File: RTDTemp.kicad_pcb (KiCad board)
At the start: 2 copper layers, 114.5 x 60 mm, 102 parts, among them J1 Conn_01x02, J10 Conn_01x02, J11 Conn_01x02, J2 Conn_01x02, J3 Conn_01x02, J4 CAN_In, J5 CAN_Out, J6 Conn_01x02, J7 Conn_01x02, J8 Conn_01x02, J9 Conn_01x02, U1 INA21x, U10 INA21x, U11 INA21x, U12 INA21x, U2 Nucleo_L432KC, U3 PDS1-Sx-Sx, U4 INA21x, U5 ADM3055E, U6 INA21x, U7 CDSOT23-T24CAN, U8 INA21x, U9 INA21x

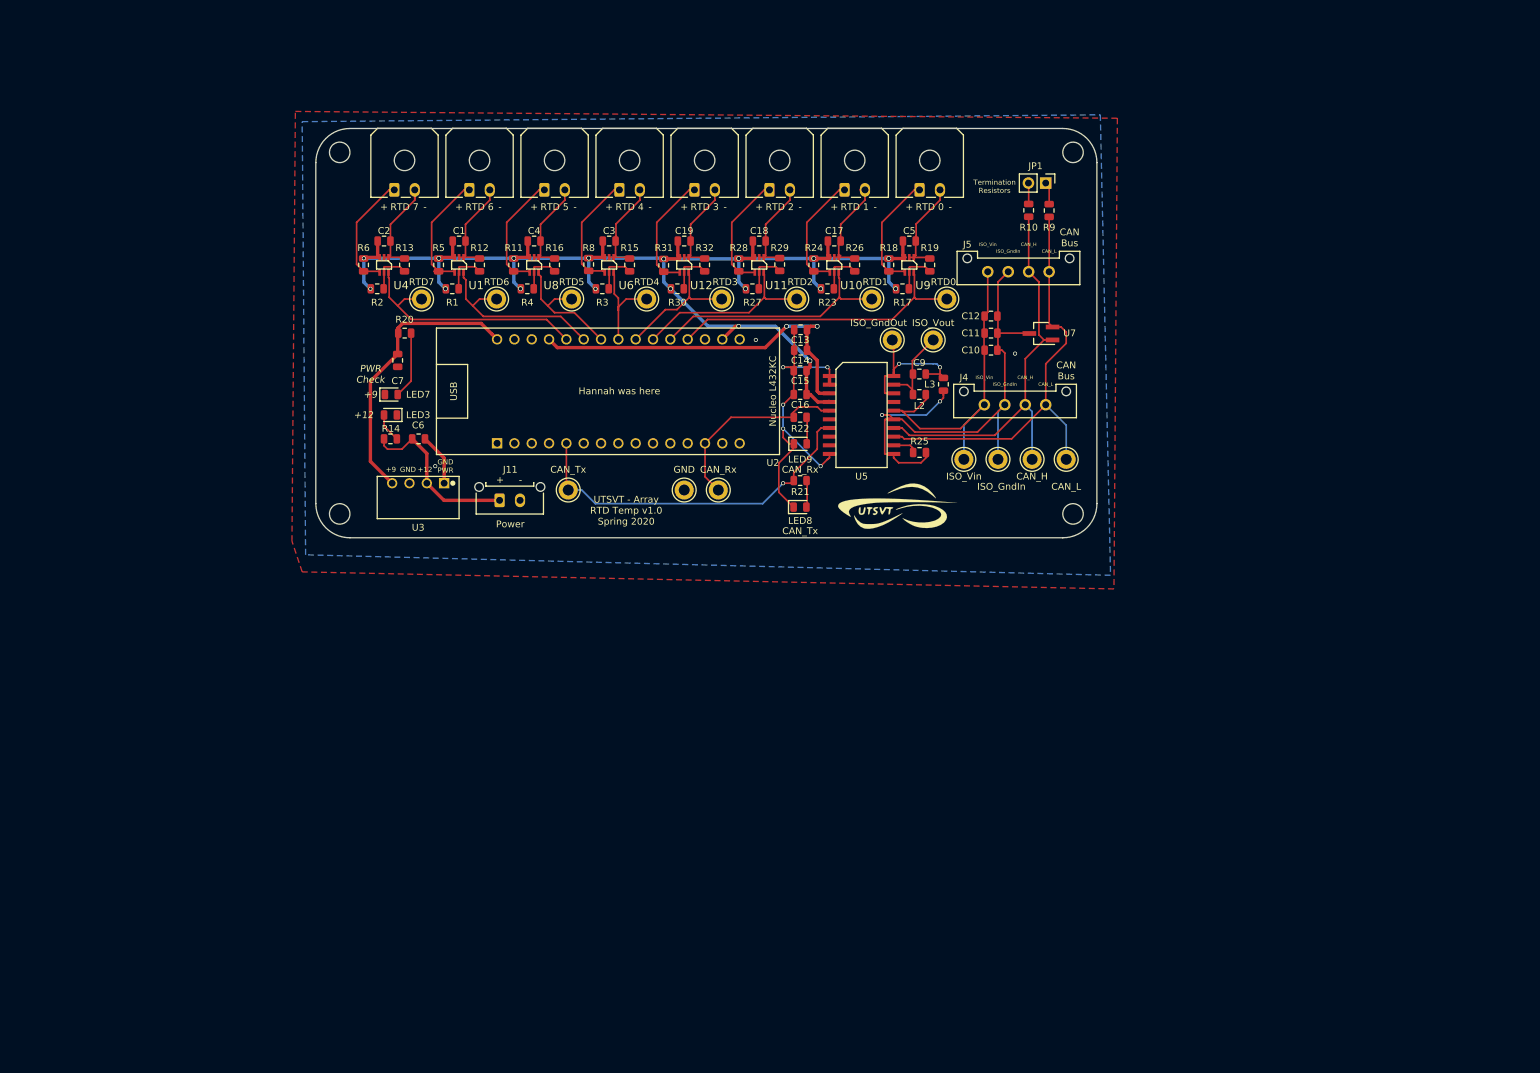
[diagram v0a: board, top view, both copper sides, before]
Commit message: Started RTD board layout update
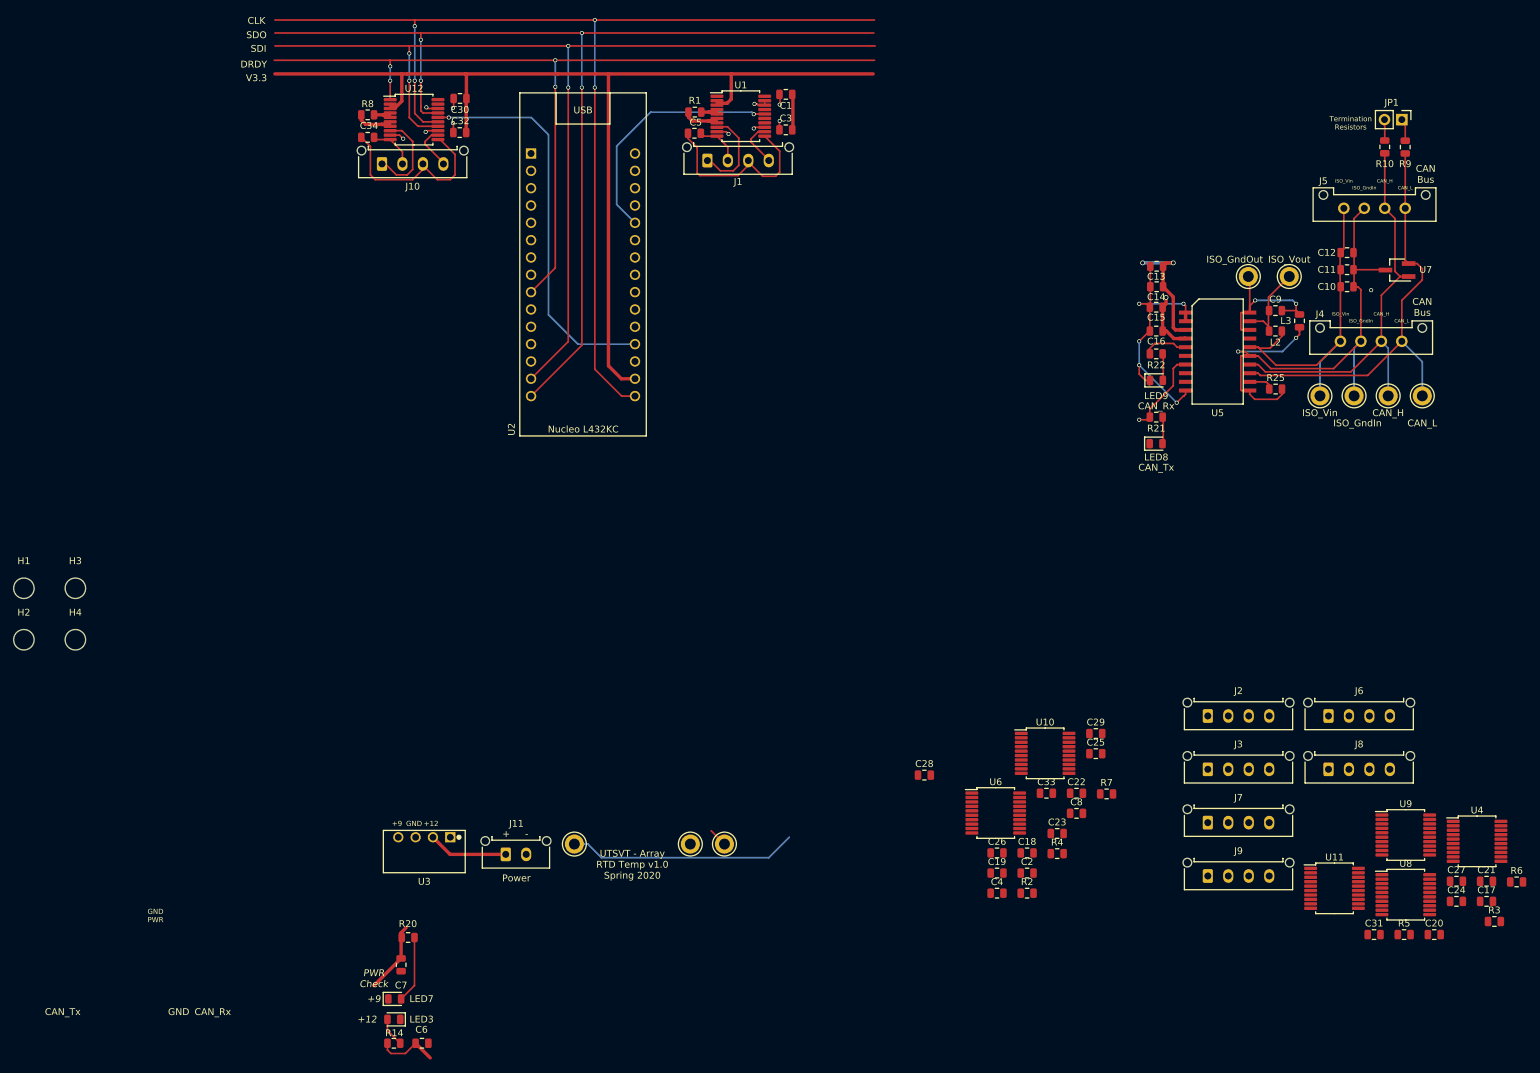
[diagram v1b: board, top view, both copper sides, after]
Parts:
- removed G***: LOGO, UTSVT_Special:Hallock_Image
- removed G***: LOGO, UTSVT_Special:UTSVT_Logo_Symbol
- removed R11, R17, R18, R23, R24, R27, R28, R30, R31: 3.3k, Resistor_SMD:R_0805_2012Metric
- removed R12, R13, R15, R16, R19, R26, R29, R32: 100, Resistor_SMD:R_0805_2012Metric
- removed RTD0, TP1, TP2, TP3, TP4, TP6, TP7, TP8: TestPoint, TestPoint:TestPoint_Keystone_5005-5009_Compact
- added C20: 100nF, Capacitor_SMD:C_0805_2012Metric, F.Cu at (266.5, 168.4)
- added C21: 100nF, Capacitor_SMD:C_0805_2012Metric, F.Cu at (274.2, 160.6)
- added C22: 100nF, Capacitor_SMD:C_0805_2012Metric, F.Cu at (214.1, 147.7)
- added C23: 100nF, Capacitor_SMD:C_0805_2012Metric, F.Cu at (211.2, 153.6)
- added C24: 100nF, Capacitor_SMD:C_0805_2012Metric, F.Cu at (269.8, 163.5)
- added C25: 100nF, Capacitor_SMD:C_0805_2012Metric, F.Cu at (216.9, 141.9)
- added C26: 100nF, Capacitor_SMD:C_0805_2012Metric, F.Cu at (202.4, 156.4)
- added C27: 100nF, Capacitor_SMD:C_0805_2012Metric, F.Cu at (269.8, 160.6)
- added C28: 100nF, Capacitor_SMD:C_0805_2012Metric, F.Cu at (191.8, 145.0)
- added C29: 100nF, Capacitor_SMD:C_0805_2012Metric, F.Cu at (216.9, 138.9)
- added C30: 100nF, Capacitor_SMD:C_0805_2012Metric, F.Cu at (123.7, 45.8)
- added C31: 100nF, Capacitor_SMD:C_0805_2012Metric, F.Cu at (257.7, 168.4)
- added C32: 100nF, Capacitor_SMD:C_0805_2012Metric, F.Cu at (123.7, 50.8)
- added C33: 100nF, Capacitor_SMD:C_0805_2012Metric, F.Cu at (209.7, 147.7)
- added C34: 100nF, Capacitor_SMD:C_0805_2012Metric, F.Cu at (110.2, 51.5)
- added C8: 100nF, Capacitor_SMD:C_0805_2012Metric, F.Cu at (214.1, 150.6)
- added R7: 400, Resistor_SMD:R_0805_2012Metric, F.Cu at (218.5, 147.8)
- C1, C17, C18, C19, C2, C3, C4, C5: value .1u -> 100nF
- J1, J10, J2, J3, J6, J7, J8, J9: value Conn_01x02 -> Conn_01x04; footprint Connector_Molex:Molex_Micro-Fit_3.0_43650-0200_1x02_P3.00mm_Horizontal -> Connector_Molex:Molex_Micro-Fit_3.0_43650-0415_1x04_P3.00mm_Vertical
- R1, R2, R3, R4, R5, R6, R8: value 3.3k -> 400
- U1, U10, U11, U12, U4, U6, U8, U9: value INA21x -> MAX31865xAP; footprint UTSVT_ICs:SOIC-6_1.40x2.15mm_Pitch0.65mm -> Package_SO:SSOP-20_5.3x7.2mm_P0.65mm
- moved R6 191.7 mm to (278.6, 160.7), turned to 0 degrees
- moved U4 181.1 mm to (272.8, 154.7), turned to 0 degrees
- moved R5 172.3 mm to (262.1, 168.4), turned to 0 degrees
- moved H2 169.6 mm to (59.8, 125.2)
- moved R3 160.3 mm to (275.3, 166.5), turned to 0 degrees
- moved U8 157.6 mm to (262.3, 162.5), turned to 0 degrees
- moved H4 147.4 mm to (67.3, 125.2)
- moved J2 142.0 mm to (233.3, 136.3)
- moved J6 138.4 mm to (251.0, 136.3)
- moved C17 136.1 mm to (274.2, 163.5), turned to 0 degrees
- moved C2 132.2 mm to (206.8, 159.4), turned to 0 degrees
- moved R2 130.1 mm to (206.8, 162.3), turned to 0 degrees
- moved U11 124.4 mm to (251.9, 161.6), turned to 0 degrees
- moved J3 121.1 mm to (233.3, 144.2)
- moved J9 119.4 mm to (233.3, 159.8)
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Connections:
- C1 pad 1: GND -> +3V3
- C1 pad 2: +3V3 -> GND
- C17 pad 1: GND -> +3V3
- C17 pad 2: +3V3 -> GND
- C18 pad 1: GND -> +3V3
- C18 pad 2: +3V3 -> GND
- C19 pad 1: GND -> +3V3
- C19 pad 2: +3V3 -> GND
- C2 pad 1: GND -> +3V3
- C2 pad 2: +3V3 -> GND
- C3 pad 1: GND -> +3V3
- C3 pad 2: +3V3 -> GND
- C4 pad 1: GND -> +3V3
- C4 pad 2: +3V3 -> GND
- C5 pad 1: GND -> Net-(C5-Pad1)
- C5 pad 2: +3V3 -> Net-(C5-Pad2)
- J1 pad 2: GND -> Net-(C5-Pad1)
- J10 pad 2: GND -> Net-(C34-Pad1)
- J2 pad 2: GND -> Net-(C8-Pad1)
- J3 pad 2: GND -> Net-(C21-Pad1)
- J6 pad 2: GND -> Net-(C22-Pad1)
- J7 pad 2: GND -> Net-(C27-Pad1)
- J8 pad 2: GND -> Net-(C28-Pad1)
- J9 pad 2: GND -> Net-(C33-Pad1)
- R1 pad 2: +3V3 -> Net-(R1-Pad2)
- R2 pad 1: Net-(R13-Pad2) -> Net-(R2-Pad1)
- R2 pad 2: +3V3 -> Net-(R2-Pad2)
- R3 pad 1: Net-(R15-Pad2) -> Net-(R3-Pad1)
- R3 pad 2: +3V3 -> Net-(R3-Pad2)
- R4 pad 1: Net-(R16-Pad2) -> Net-(R4-Pad1)
- R4 pad 2: +3V3 -> Net-(R4-Pad2)
- R5 pad 1: Net-(J1-Pad1) -> Net-(R5-Pad1)
- R5 pad 2: +3V3 -> Net-(R5-Pad2)
- R6 pad 1: Net-(J2-Pad1) -> Net-(R6-Pad1)
- R6 pad 2: +3V3 -> Net-(R6-Pad2)
- R8 pad 1: Net-(J3-Pad1) -> Net-(R8-Pad1)
- R8 pad 2: +3V3 -> Net-(R8-Pad2)
- U1 pad 1: GND -> DRDY
- U1 pad 2: GND -> +3V3
- U1 pad 4: Net-(J1-Pad1) -> Net-(R1-Pad1)
- U1 pad 6: /RTD6 -> Net-(R1-Pad2)
- U10 pad 1: GND -> DRDY
- U10 pad 2: GND -> +3V3
- U10 pad 4: Net-(J8-Pad1) -> Net-(R6-Pad1)
- U10 pad 5: Net-(R23-Pad1) -> Net-(R6-Pad1)
- U10 pad 6: /RTD1 -> Net-(R6-Pad2)
- U11 pad 1: GND -> DRDY
- U11 pad 2: GND -> +3V3
- U11 pad 4: Net-(J9-Pad1) -> Net-(R7-Pad1)
- U11 pad 5: Net-(R27-Pad1) -> Net-(R7-Pad1)
- U11 pad 6: /RTD2 -> Net-(R7-Pad2)
- U12 pad 1: GND -> DRDY
- U12 pad 2: GND -> +3V3
- U12 pad 4: Net-(J10-Pad1) -> Net-(R8-Pad1)
- U12 pad 5: Net-(R30-Pad1) -> Net-(R8-Pad1)
- U12 pad 6: /RTD3 -> Net-(R8-Pad2)
- U2 pad 14: Net-(U2-Pad14) -> SDI
- U2 pad 15: Net-(U2-Pad15) -> SDO
- U2 pad 16: Net-(U2-Pad16) -> CLK
- U2 pad 19: /RTD0 -> CS_0
- U2 pad 20: /RTD1 -> CS_1
- U2 pad 21: /RTD2 -> CS_2
- U2 pad 22: /RTD3 -> CS_3
- U2 pad 23: /RTD4 -> CS_4
- U2 pad 24: /RTD5 -> CS_5
- U2 pad 25: /RTD6 -> CS_6
- U2 pad 26: /RTD7 -> CS_7
- U2 pad 9: Net-(U2-Pad9) -> DRDY
- U4 pad 1: GND -> DRDY
- U4 pad 2: GND -> +3V3
- U4 pad 4: Net-(J2-Pad1) -> Net-(R2-Pad1)
- U4 pad 5: Net-(R13-Pad2) -> Net-(R2-Pad1)
- U4 pad 6: /RTD7 -> Net-(R2-Pad2)
- U6 pad 1: GND -> DRDY
- U6 pad 2: GND -> +3V3
- U6 pad 4: Net-(J3-Pad1) -> Net-(R3-Pad1)
- U6 pad 5: Net-(R15-Pad2) -> Net-(R3-Pad1)
- U6 pad 6: /RTD4 -> Net-(R3-Pad2)
- U8 pad 1: GND -> DRDY
- U8 pad 2: GND -> +3V3
- U8 pad 4: Net-(J6-Pad1) -> Net-(R4-Pad1)
- U8 pad 5: Net-(R16-Pad2) -> Net-(R4-Pad1)
- U8 pad 6: /RTD5 -> Net-(R4-Pad2)
- U9 pad 1: GND -> DRDY
- U9 pad 2: GND -> +3V3
- U9 pad 4: Net-(J7-Pad1) -> Net-(R5-Pad1)
- U9 pad 5: Net-(R17-Pad1) -> Net-(R5-Pad1)
- U9 pad 6: /RTD0 -> Net-(R5-Pad2)
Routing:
- net CLK: track 0.00 -> 164.2 mm, vias 0 -> 4
- net SDO: track 0.00 -> 158.2 mm, vias 0 -> 4
- net SDI: track 0.00 -> 154.2 mm, vias 0 -> 4
- net DRDY: track 0.00 -> 129.2 mm, vias 0 -> 4
- net GND: track 171.8 -> 58.8 mm, vias 8 -> 16
- net CS_0: track 0.00 -> 58.1 mm, vias 0 -> 1
- net /RTD0: track 44.3 -> 0.00 mm
- net +5V: track 54.4 -> 17.8 mm
- net CS_7: track 0.00 -> 36.2 mm, vias 0 -> 1
- net /RTD7: track 36.1 -> 0.00 mm
- net /RTD1: track 35.9 -> 0.00 mm
- net +9VA: track 41.7 -> 10.6 mm
- net Net-(C34-Pad2): track 0.00 -> 27.9 mm
- net /RTD6: track 27.7 -> 0.00 mm
- net Net-(C5-Pad2): track 0.00 -> 27.4 mm
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- removed copper zone on B.Cu, net GND
- removed copper zone on F.Cu, net GND
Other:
- board outline removed
- board text added: "CLK"
- board text added: "DRDY"
- board text added: "SDI"
- board text added: "SDO"
- board text added: "V3.3"
- board text removed: "Hannah was here"
- board text removed: "RTD 0"
- board text removed: "RTD 1"
- board text removed: "RTD 2"
- board text removed: "RTD 3"
- board text removed: "RTD 4"
- board text removed: "RTD 5"
- board text removed: "RTD 6"
- board text removed: "RTD 7"
- board text removed: "RTD1"
- board text removed: "RTD2"
- board text removed: "RTD3"
- board text removed: "RTD4"
- board text removed: "RTD5"
- board text removed: "RTD6"
- board text removed: "RTD7"
